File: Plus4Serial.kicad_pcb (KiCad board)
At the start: 2 copper layers, 54 x 47.5 mm, 11 parts, among them CN1 C64-User-Port-Female, CN2 DB9_MALE, U1 MC1489, U2 MC1488

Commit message: Fix some errors
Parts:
- CN1: value C64-User-Port-Female -> PLUS4_USERPORT
- moved C1 0.64 mm to (160.1, 102.7)
- moved C2 0.64 mm to (150.0, 102.7)
- moved C3 0.64 mm to (135.3, 102.7)
- moved C4 0.64 mm to (152.3, 88.8)
- moved D1 0.64 mm to (172.0, 100.1)
- moved D2 0.64 mm to (167.4, 107.7)
- moved D3 0.64 mm to (142.6, 100.1)
- moved U1 0.63 mm to (157.0, 95.1)
- moved U2 0.63 mm to (132.3, 95.1)
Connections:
- net /_dcd renamed /_~dcd
- CN1 pad 3: Net-(CN1-Pad3) -> (no net)
- CN1 pad 4: Net-(CN1-Pad4) -> (no net)
- CN1 pad 5: Net-(CN1-Pad5) -> (no net)
- CN1 pad 6: Net-(CN1-Pad6) -> (no net)
- CN1 pad 7: Net-(CN1-Pad7) -> (no net)
- CN1 pad 8: /rxc -> (no net)
- CN1 pad 9: Net-(CN1-Pad9) -> (no net)
- CN1 pad B: /~cts -> (no net)
- CN1 pad F: Net-(CN1-PadF) -> (no net)
- CN1 pad J: Net-(CN1-PadJ) -> (no net)
- CN1 pad K: Net-(CN1-PadK) -> /~cts
- CN2 pad 9: /_ri -> (no net)
- U1 pad 11: /~dsr -> /~dcd
- U1 pad 12: Net-(U1-Pad12) -> (no net)
- U1 pad 2: Net-(U1-Pad2) -> (no net)
- U1 pad 5: Net-(U1-Pad5) -> (no net)
- U1 pad 9: Net-(U1-Pad9) -> (no net)
- U2 pad 3: Net-(U2-Pad3) -> (no net)
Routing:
- net /~dcd: track 0.00 -> 45.0 mm, vias 0 -> 2
- net /~cts: track 18.6 -> 47.6 mm, vias 0 -> 2
- net /~dsr: track 63.6 -> 62.9 mm
- net +5V: track 75.3 -> 75.9 mm
- net /~dtr: track 44.8 -> 45.5 mm
- net /_~dsr: track 17.8 -> 17.1 mm
- net /txd: track 40.5 -> 41.2 mm
- net /_~rts: track 22.2 -> 21.5 mm
- net /~rts: track 39.3 -> 39.9 mm
- net /rxd: track 20.2 -> 20.8 mm
- net /_~cts: track 28.4 -> 27.8 mm
- net /_rxd: track 16.4 -> 15.8 mm

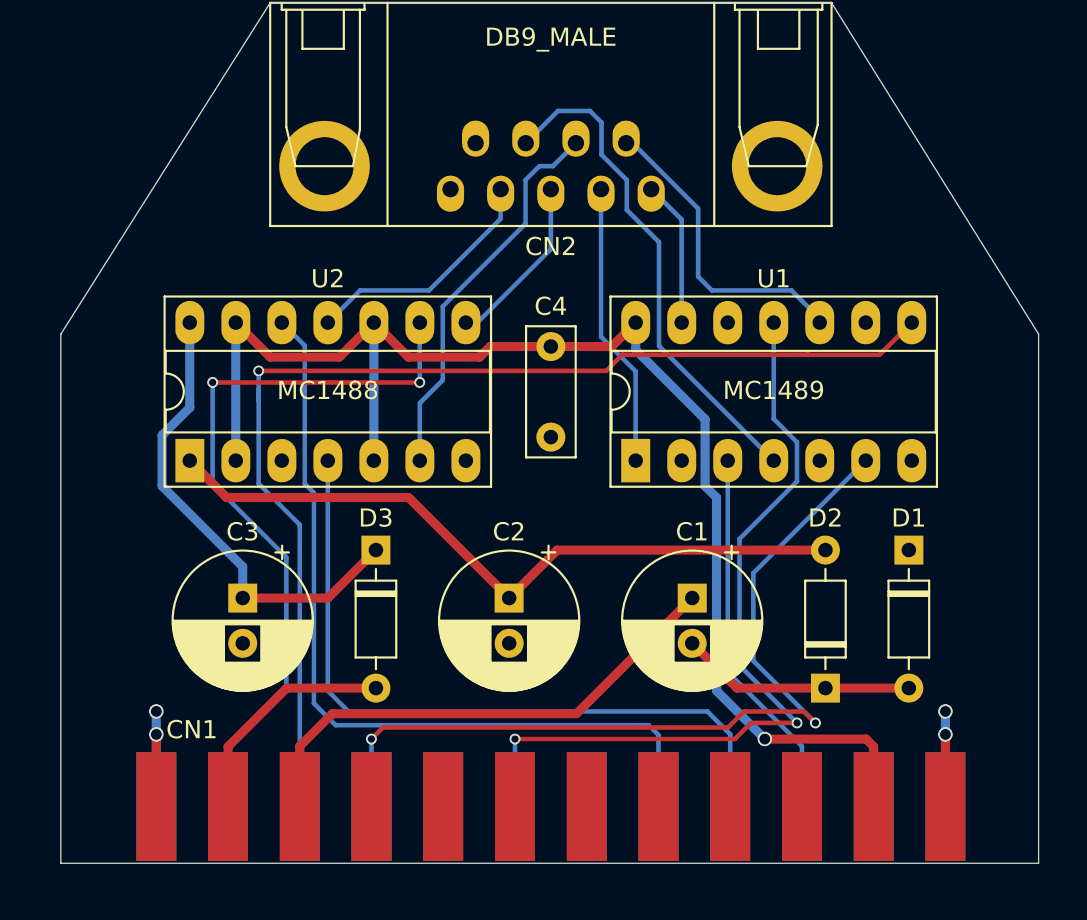
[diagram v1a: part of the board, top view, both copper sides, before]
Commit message: Switch to MAX238
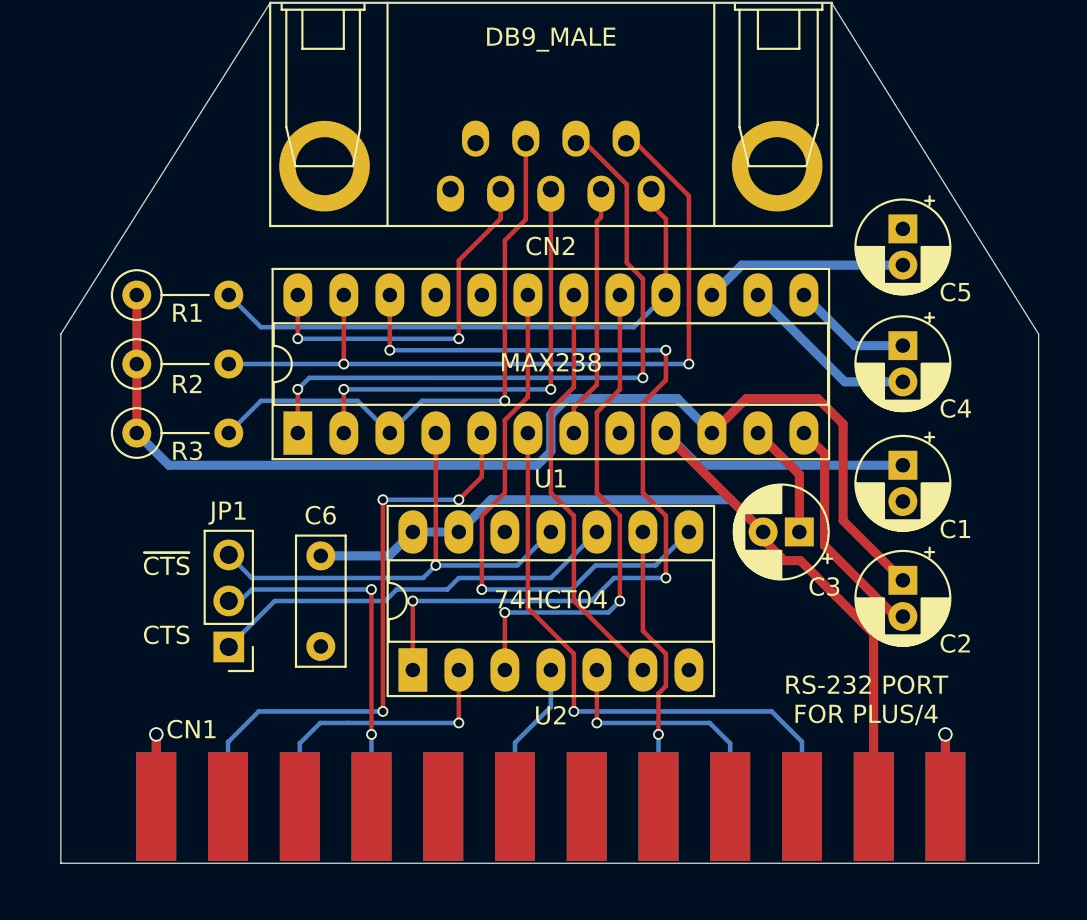
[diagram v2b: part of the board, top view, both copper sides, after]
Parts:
- removed D1, D2, D3: 1N4148, Diode_THT:D_DO-35_SOD27_P7.62mm_Horizontal
- added C5: 1u, Capacitor_THT:CP_Radial_D5.0mm_P2.00mm, F.Cu at (171.7, 82.3)
- added C6: 100n, Capacitor_THT:C_Disc_D7.0mm_W2.5mm_P5.00mm, F.Cu at (139.6, 100.4)
- added JP1: JMP_CTS, Connector_PinHeader_2.54mm:PinHeader_1x03_P2.54mm_Vertical, F.Cu at (134.5, 105.4)
- added R1: 10k, Resistor_THT:R_Axial_DIN0207_L6.3mm_D2.5mm_P5.08mm_Vertical, F.Cu at (129.4, 86.0)
- added R2: 10k, Resistor_THT:R_Axial_DIN0207_L6.3mm_D2.5mm_P5.08mm_Vertical, F.Cu at (129.4, 89.8)
- added R3: 10k, Resistor_THT:R_Axial_DIN0207_L6.3mm_D2.5mm_P5.08mm_Vertical, F.Cu at (129.4, 93.6)
- C1, C2, C3: value 100u -> 1u; footprint Capacitor_THT:CP_Radial_D7.5mm_P2.50mm -> Capacitor_THT:CP_Radial_D5.0mm_P2.00mm
- C4: value 100n -> 1u; footprint Capacitor_THT:C_Disc_D7.0mm_W2.5mm_P5.00mm -> Capacitor_THT:CP_Radial_D5.0mm_P2.00mm
- U1: value MC1489 -> MAX238; footprint Package_DIP:DIP-14_W7.62mm_Socket_LongPads -> Package_DIP:DIP-24_W7.62mm_Socket_LongPads
- U2: value MC1488 -> 74HCT04
- moved C3 30.9 mm to (166.0, 99.1), turned to 180 degrees
- moved C2 21.8 mm to (171.7, 101.7)
- moved C4 19.4 mm to (171.7, 88.8)
- moved U1 18.7 mm to (138.3, 93.6)
- moved U2 16.9 mm to (144.7, 106.7)
- moved C1 13.7 mm to (171.7, 95.4)
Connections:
- C1 pad 1: +9VA -> +5V
- C1 pad 2: Net-(C1-Pad2) -> GND
- C2 pad 1: -12V -> +12V
- C2 pad 2: GND -> Net-(C2-Pad2)
- C3 pad 1: +12V -> Net-(C3-Pad1)
- C3 pad 2: GND -> +5V
- C4 pad 1: +5V -> Net-(C4-Pad1)
- C4 pad 2: GND -> Net-(C4-Pad2)
- CN1 pad 10: +9VA -> (no net)
- CN1 pad 11: -9VA -> (no net)
- CN1 pad C: /rxd -> /rxd_ttl
- CN1 pad D: /~rts -> /rts_ttl
- CN1 pad E: /~dtr -> /dtr_ttl
- CN1 pad H: /~dcd -> /dcd_ttl
- CN1 pad K: /~cts -> /~cts_ttl
- CN1 pad L: /~dsr -> /dsr_ttl
- CN1 pad M: /txd -> /txd_ttl
- CN2 pad 1: /_~dcd -> /~dcd
- CN2 pad 2: /_rxd -> /rxd
- CN2 pad 3: /_txd -> /txd
- CN2 pad 4: /_~dtr -> /~dtr
- CN2 pad 6: /_~dsr -> /~dsr
- CN2 pad 7: /_~rts -> /~rts
- CN2 pad 8: /_~cts -> /~cts
- U1 pad 1: /_rxd -> /~rts
- U1 pad 10: /_~dsr -> +12V
- U1 pad 11: /~dcd -> Net-(C3-Pad1)
- U1 pad 12: (no net) -> Net-(C2-Pad2)
- U1 pad 13: /_~dcd -> Net-(C4-Pad1)
- U1 pad 14: +5V -> Net-(C4-Pad2)
- U1 pad 2: (no net) -> /txd
- U1 pad 3: /rxd -> /~cts
- U1 pad 4: /_~cts -> Net-(JP1-Pad3)
- U1 pad 5: (no net) -> /txd_ttl
- U1 pad 6: /~cts -> /rxd_ttl
- U1 pad 7: GND -> /rxd
- U1 pad 8: /~dsr -> GND
- U1 pad 9: (no net) -> +5V
- U2 pad 1: -12V -> Net-(U1-Pad22)
- U2 pad 10: +5V -> Net-(JP1-Pad1)
- U2 pad 11: /_~dtr -> Net-(JP1-Pad3)
- U2 pad 12: /~dtr -> (no net)
- U2 pad 14: +12V -> +5V
- U2 pad 2: +5V -> /dsr_ttl
- U2 pad 3: (no net) -> Net-(U1-Pad17)
- U2 pad 4: /~rts -> /dcd_ttl
- U2 pad 5: +5V -> /rts_ttl
- U2 pad 6: /_~rts -> Net-(U1-Pad18)
- U2 pad 8: /_txd -> Net-(U1-Pad19)
- U2 pad 9: /txd -> /dtr_ttl
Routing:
- net Net-(U1-Pad22): track 0.00 -> 50.2 mm, vias 0 -> 4
- net -12V: track 39.3 -> 0.00 mm
- net +12V: track 26.1 -> 62.2 mm
- net /rxd_ttl: track 0.00 -> 33.3 mm, vias 0 -> 1
- net /txd_ttl: track 0.00 -> 32.9 mm, vias 0 -> 3
- net Net-(U1-Pad19): track 0.00 -> 30.1 mm, vias 0 -> 1
- net +9VA: track 28.4 -> 0.00 mm
- net /_~cts: track 27.8 -> 0.00 mm
- net Net-(U1-Pad17): track 0.00 -> 27.7 mm, vias 0 -> 2
- net Net-(JP1-Pad3): track 0.00 -> 26.8 mm, vias 0 -> 1
- net /~dtr: track 45.5 -> 20.5 mm, vias 0 -> 2
- net Net-(U1-Pad18): track 0.00 -> 23.3 mm
- net Net-(JP1-Pad1): track 0.00 -> 22.9 mm
- net /_~rts: track 21.5 -> 0.00 mm
- net /~cts_ttl: track 0.00 -> 20.1 mm, vias 0 -> 2
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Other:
- board text added: "CC-BY-NC-SA © SukkoPera 2022 github.com/SukkoPera/Plus4Serial"
- board text added: "CTS"
- board text added: "RS-232 PORT FOR PLUS/4"
- board text added: "~CTS~"

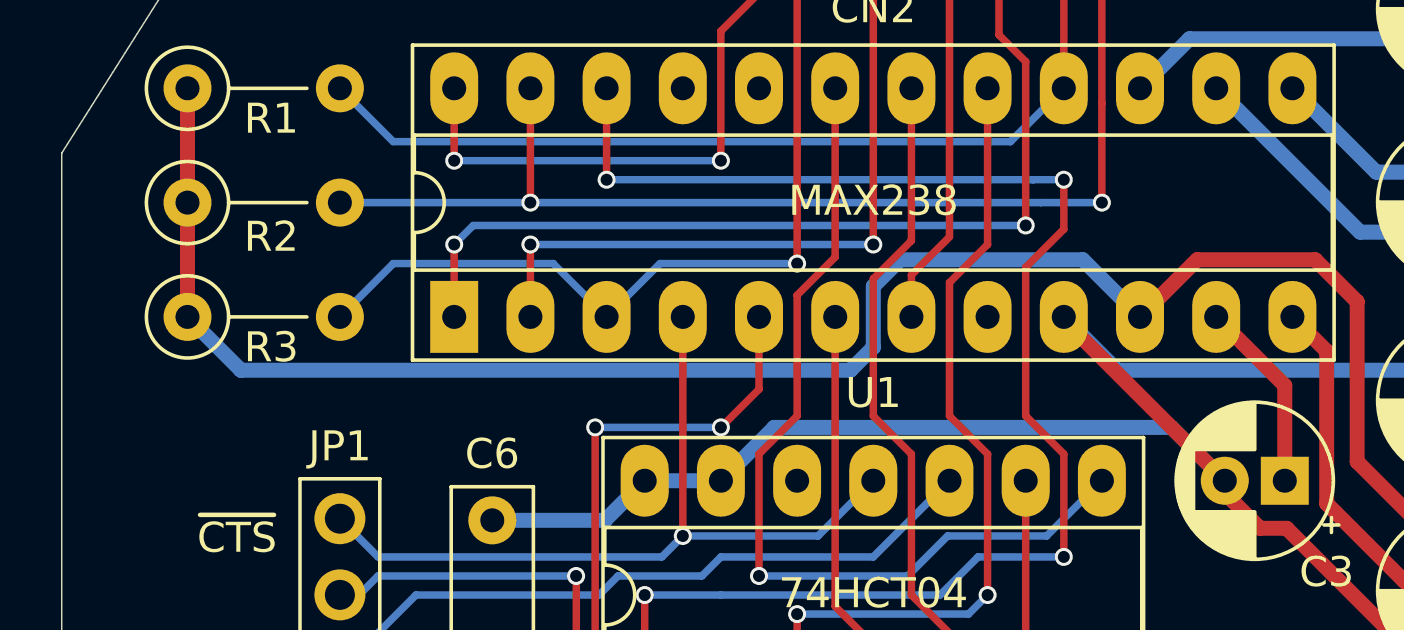
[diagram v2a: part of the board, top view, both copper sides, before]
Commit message: Take +12V from correct pin
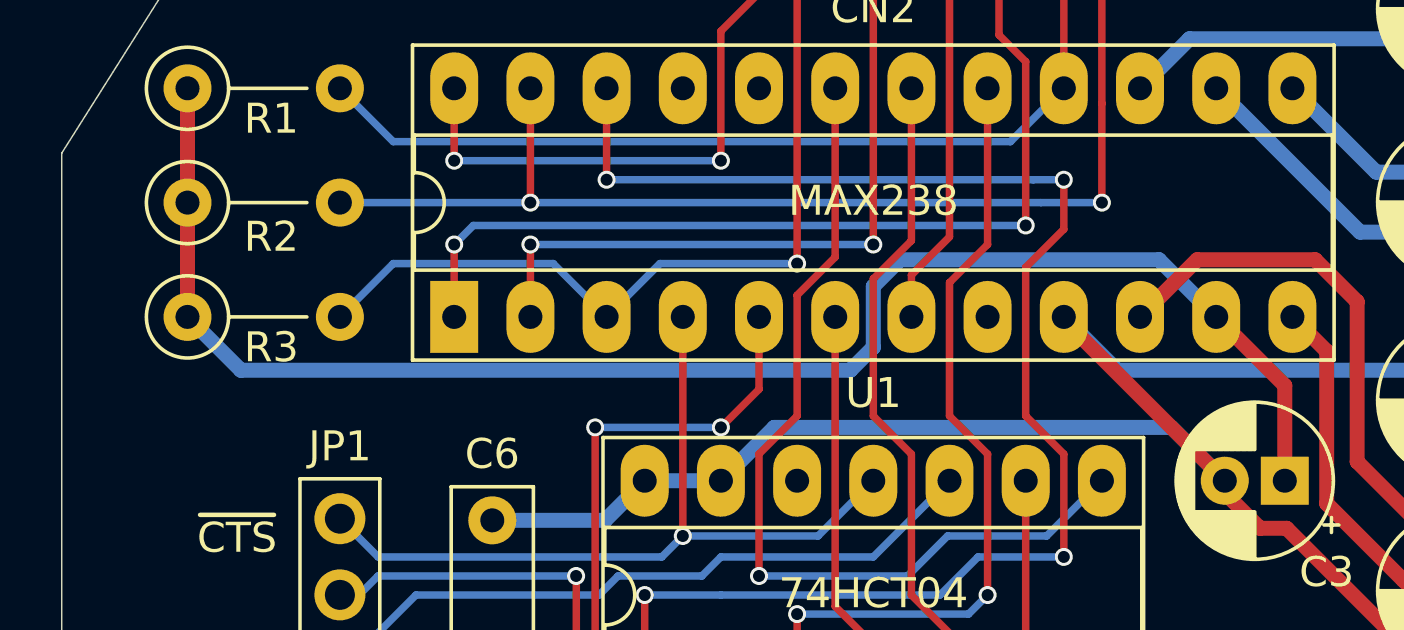
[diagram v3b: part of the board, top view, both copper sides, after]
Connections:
- C2 pad 1: +12V -> Net-(C2-Pad1)
- C3 pad 1: Net-(C3-Pad1) -> +12V
- U1 pad 10: +12V -> Net-(C2-Pad1)
- U1 pad 11: Net-(C3-Pad1) -> +12V
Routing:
- net Net-(C2-Pad1): track 0.00 -> 18.6 mm
- net +12V: track 62.2 -> 52.6 mm
- net Net-(C3-Pad1): track 6.41 -> 0.00 mm

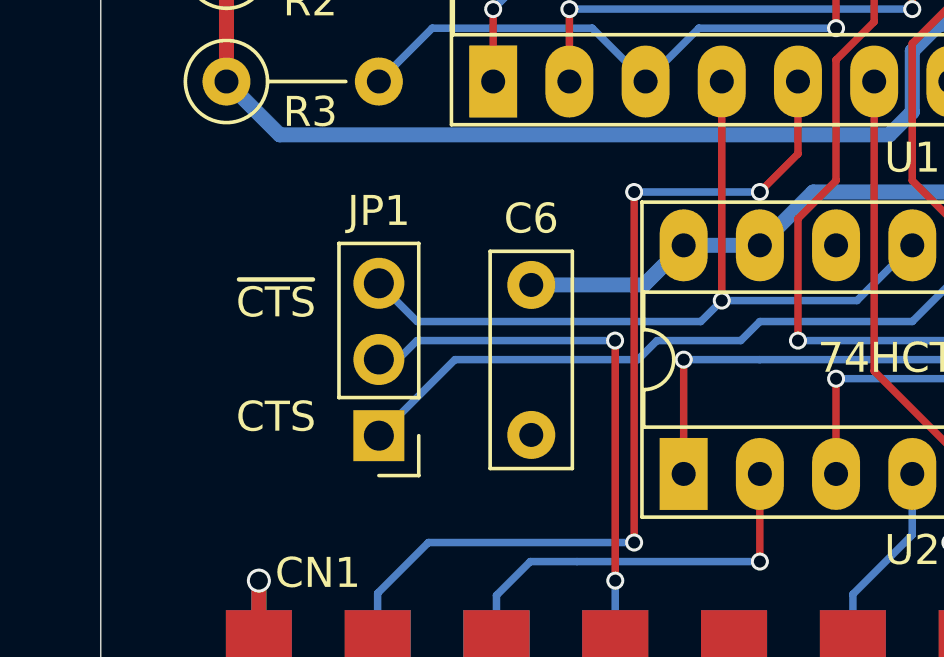
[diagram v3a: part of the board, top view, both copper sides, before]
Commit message: Remove CTS/_CTS jumper Now we know for certain that CTS is active-high on the User Port
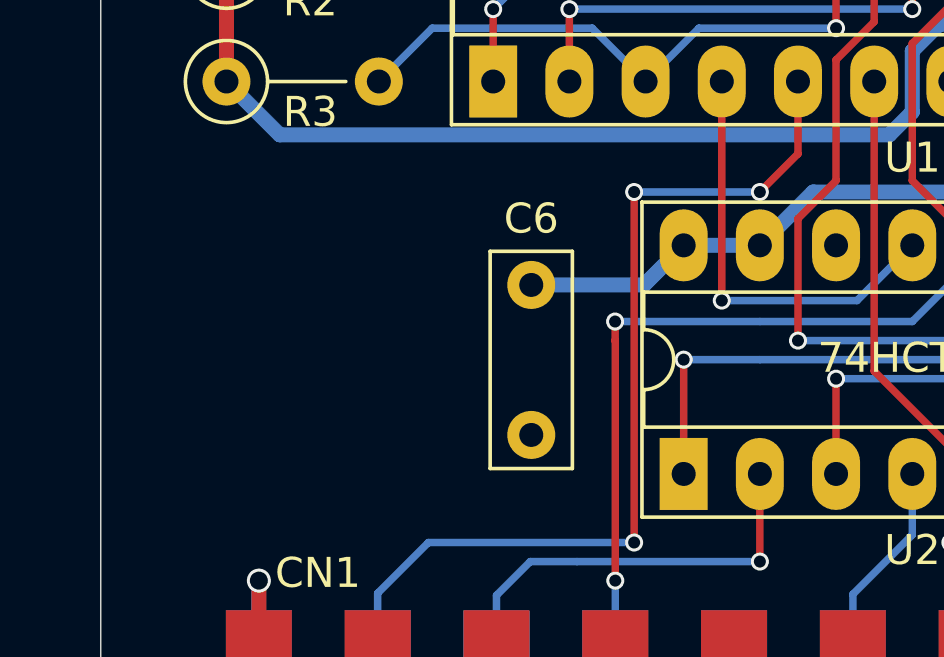
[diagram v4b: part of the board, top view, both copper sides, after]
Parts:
- removed JP1: JMP_CTS, Connector_PinHeader_2.54mm:PinHeader_1x03_P2.54mm_Vertical
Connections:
- CN1 pad 10: (no net) -> Net-(CN1-Pad10)
- CN1 pad 11: (no net) -> Net-(CN1-Pad11)
- CN1 pad 3: (no net) -> Net-(CN1-Pad3)
- CN1 pad 4: (no net) -> Net-(CN1-Pad4)
- CN1 pad 5: (no net) -> Net-(CN1-Pad5)
- CN1 pad 6: (no net) -> Net-(CN1-Pad6)
- CN1 pad 7: (no net) -> Net-(CN1-Pad7)
- CN1 pad 8: (no net) -> /rxc
- CN1 pad 9: (no net) -> Net-(CN1-Pad9)
- CN1 pad B: (no net) -> Net-(CN1-PadB)
- CN1 pad F: (no net) -> Net-(CN1-PadF)
- CN1 pad J: (no net) -> Net-(CN1-PadJ)
- CN1 pad K: /~cts_ttl -> /cts_ttl
- CN2 pad 9: (no net) -> /_ri
- U1 pad 20: (no net) -> Net-(U1-Pad20)
- U1 pad 21: (no net) -> Net-(U1-Pad21)
- U2 pad 10: Net-(JP1-Pad1) -> /cts_ttl
- U2 pad 12: (no net) -> Net-(U2-Pad12)
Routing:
- net /cts_ttl: track 0.00 -> 26.1 mm, vias 0 -> 2
- net Net-(JP1-Pad1): track 22.9 -> 0.00 mm
- net /~cts_ttl: track 20.1 -> 0.00 mm, vias 2 -> 0
- net Net-(U1-Pad4): track 26.8 -> 14.5 mm
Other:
- board text added: "DCD"
- board text added: "DSR"
- board text added: "DTR"
- board text added: "RTS"
- board text added: "RXD"
- board text added: "TXD"
- board text added: "V2"
- board text removed: "~CTS~"
